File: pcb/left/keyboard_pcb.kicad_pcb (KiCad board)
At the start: 2 copper layers, 138.8 x 89.9 mm, 25 parts, among them J1 TRRS, K00 KEYSW, K01 KEYSW, K02 KEYSW, K03 KEYSW, K04 KEYSW, K05 KEYSW, K10 KEYSW, K11 KEYSW, K12 KEYSW, K13 KEYSW, K14 KEYSW, K15 KEYSW, K20 KEYSW, K21 KEYSW, K22 KEYSW, K23 KEYSW, K24 KEYSW, K25 KEYSW, K30 KEYSW, K31 KEYSW, K32 KEYSW, U2 Pico

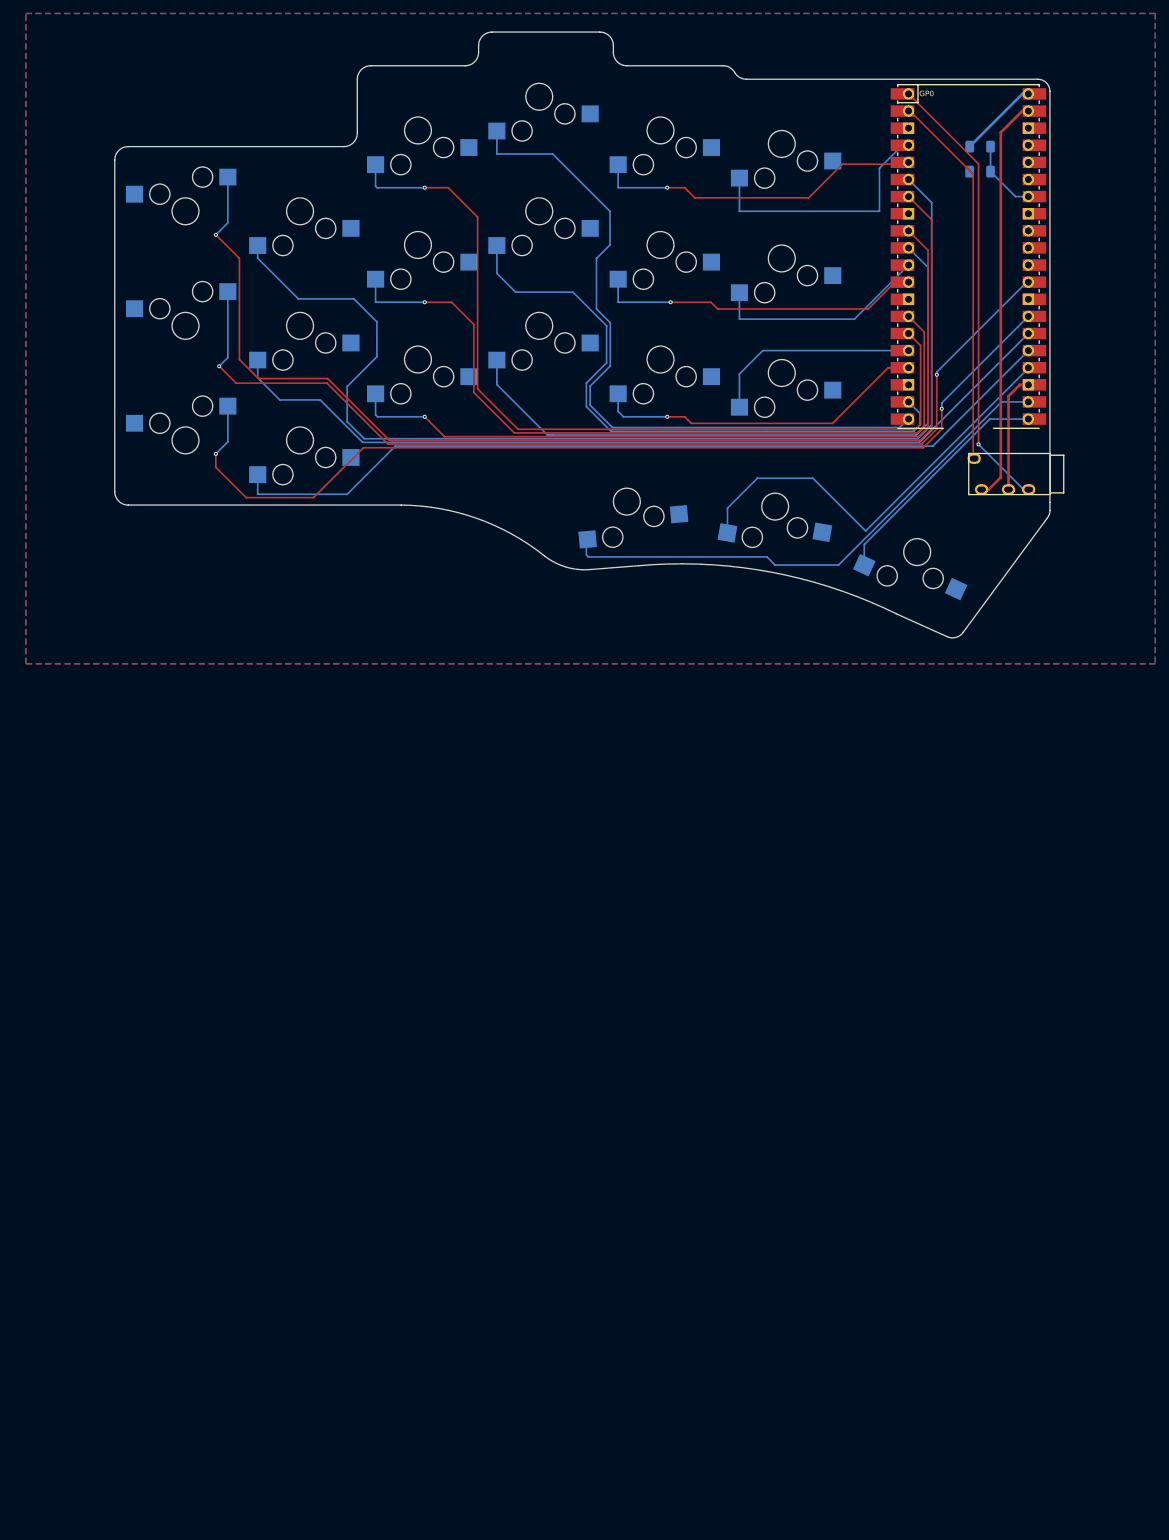
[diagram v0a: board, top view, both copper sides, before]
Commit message: feat: add right side pcb
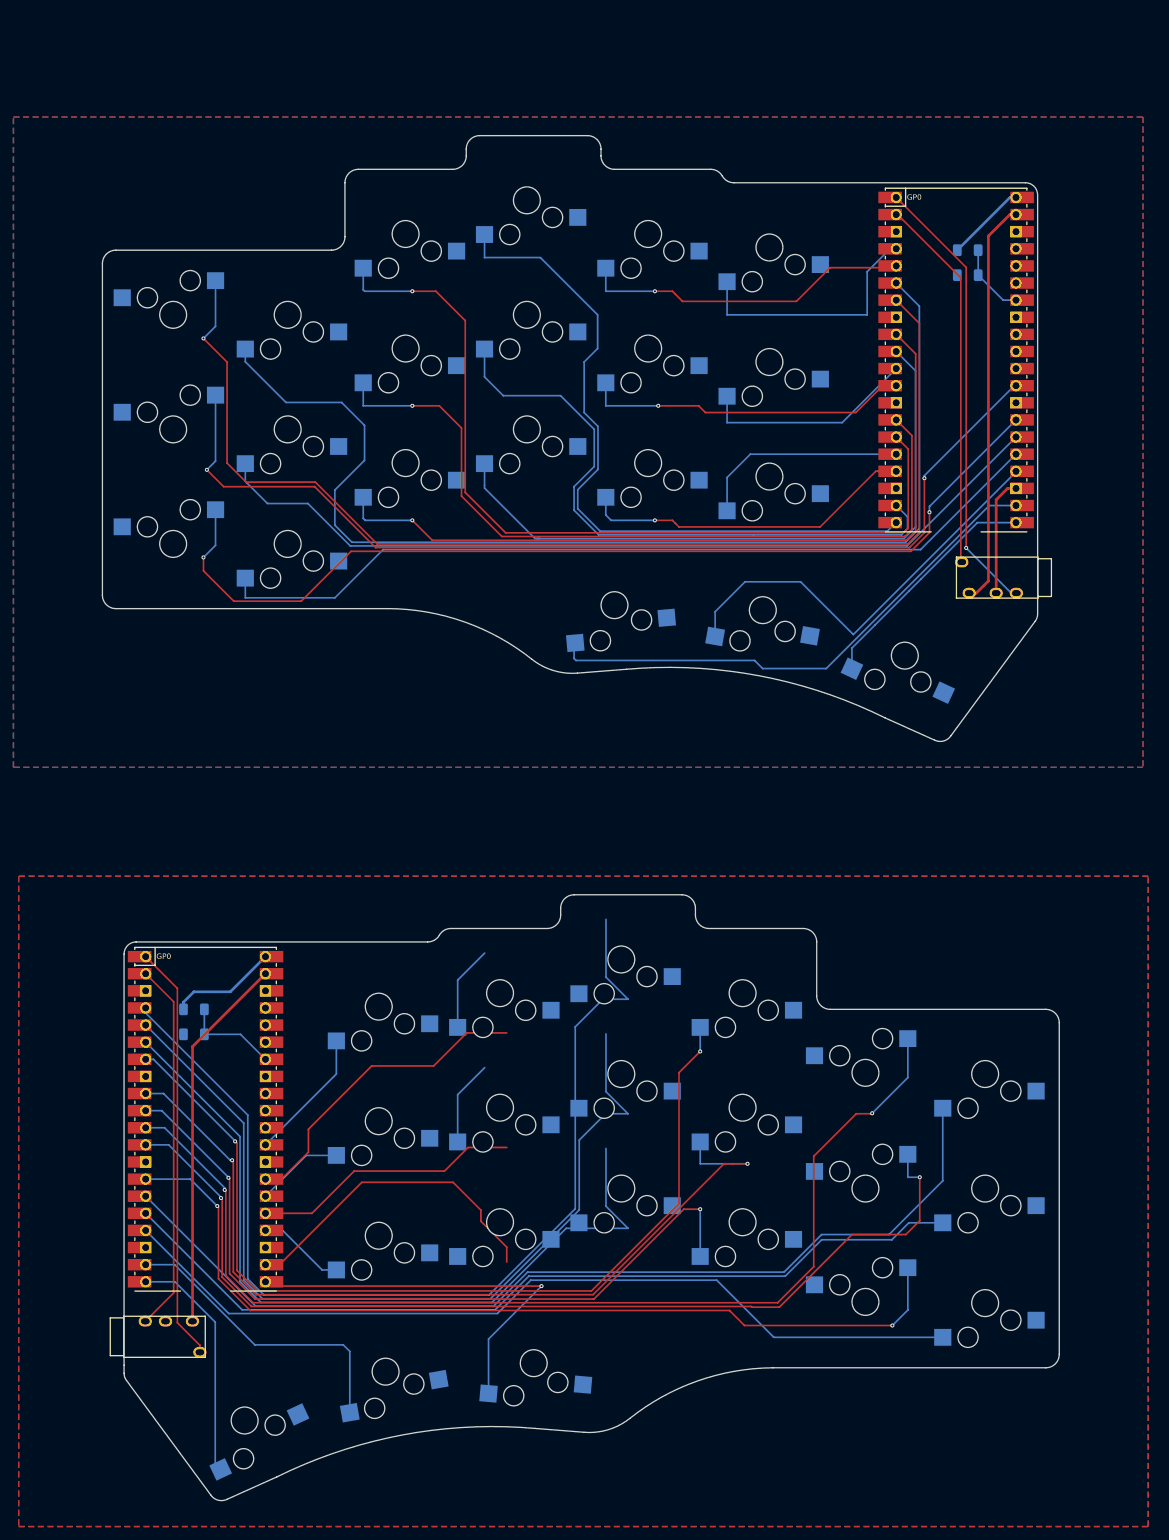
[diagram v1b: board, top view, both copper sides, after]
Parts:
- added J1: TRRS, Keebio-Parts:TRRS-PJ-320A, F.Cu at (37.4, 213.2)
- added K00: KEYSW, keyswitches:Kailh_socket_MX_3_pins_last, F.Cu at (166.3, 174.2)
- added K01: KEYSW, keyswitches:Kailh_socket_MX_3_pins_last, F.Cu at (146.5, 174.0)
- added K02: KEYSW, keyswitches:Kailh_socket_MX_3_pins_last, F.Cu at (130.3, 162.2)
- added K03: KEYSW, keyswitches:Kailh_socket_MX_3_pins_last, F.Cu at (112.3, 157.2)
- added K04: KEYSW, keyswitches:Kailh_socket_MX_3_pins_last, F.Cu at (94.3, 162.2)
- added K05: KEYSW, keyswitches:Kailh_socket_MX_3_pins_last, F.Cu at (76.3, 164.2)
- added K10: KEYSW, keyswitches:Kailh_socket_MX_3_pins_last, F.Cu at (166.3, 191.2)
- added K11: KEYSW, keyswitches:Kailh_socket_MX_3_pins_last, F.Cu at (146.5, 191.2)
- added K12: KEYSW, keyswitches:Kailh_socket_MX_3_pins_last, F.Cu at (130.3, 179.2)
- added K13: KEYSW, keyswitches:Kailh_socket_MX_3_pins_last, F.Cu at (112.3, 174.2)
- added K14: KEYSW, keyswitches:Kailh_socket_MX_3_pins_last, F.Cu at (94.3, 179.2)
- added K15: KEYSW, keyswitches:Kailh_socket_MX_3_pins_last, F.Cu at (76.3, 181.2)
- added K20: KEYSW, keyswitches:Kailh_socket_MX_3_pins_last, F.Cu at (166.3, 208.2)
- added K21: KEYSW, keyswitches:Kailh_socket_MX_3_pins_last, F.Cu at (146.5, 208.0)
- added K22: KEYSW, keyswitches:Kailh_socket_MX_3_pins_last, F.Cu at (130.3, 196.2)
- added K23: KEYSW, keyswitches:Kailh_socket_MX_3_pins_last, F.Cu at (112.3, 191.2)
- added K24: KEYSW, keyswitches:Kailh_socket_MX_3_pins_last, F.Cu at (94.3, 196.2)
- added K25: KEYSW, keyswitches:Kailh_socket_MX_3_pins_last, F.Cu at (76.3, 198.2)
- added K30: KEYSW, keyswitches:Kailh_socket_MX_3_pins_last, F.Cu at (99.3, 217.2)
- added K31: KEYSW, keyswitches:Kailh_socket_MX_3_pins_last, F.Cu at (77.3, 218.2)
- added K32: KEYSW, keyswitches:Kailh_socket_MX_3_pins_last, F.Cu at (56.3, 225.2)
- added R1: 5k6, Resistor_SMD:R_1206_3216Metric_Pad1.30x1.75mm_HandSolder, B.Cu at (47.8, 164.6)
- added R2: 10k, Resistor_SMD:R_1206_3216Metric_Pad1.30x1.75mm_HandSolder, B.Cu at (47.8, 168.3)
- added U2: Pico, RPi_Pico:RPi_Pico_SMD_TH, F.Cu at (49.6, 180.9)
- moved J1 15.5 mm to (173.1, 100.5)
- moved K20 15.5 mm to (43.8, 95.5)
- moved K21 15.5 mm to (62.8, 95.5)
- moved K22 15.5 mm to (80.2, 83.5)
- moved K24 15.5 mm to (116.2, 83.5)
- moved K25 15.5 mm to (134.2, 85.5)
- moved K30 15.5 mm to (111.2, 104.5)
- moved K31 15.5 mm to (133.2, 105.5)
- moved K32 15.5 mm to (154.2, 112.5)
- moved R1 15.5 mm to (162.7, 51.9)
- moved K00 15.5 mm to (43.8, 61.5)
- moved K01 15.5 mm to (62.8, 61.5)
- moved K02 15.5 mm to (80.2, 49.5)
- moved K03 15.5 mm to (98.2, 44.5)
- moved K04 15.5 mm to (116.2, 49.5)
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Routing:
- net /k01: track 167.1 -> 327.9 mm, vias 0 -> 2
- net /k03: track 104.6 -> 255.7 mm
- net /k11: track 127.7 -> 276.4 mm, vias 0 -> 2
- net /k00: track 173.6 -> 317.1 mm
- net /k02: track 128.5 -> 265.8 mm, vias 1 -> 3
- net /k21: track 127.3 -> 262.8 mm, vias 0 -> 2
- net /k13: track 92.4 -> 225.1 mm
- net /k12: track 116.5 -> 246.1 mm, vias 1 -> 3
- net /k10: track 151.5 -> 281.1 mm
- net /k20: track 146.7 -> 275.7 mm
- net /k23: track 99.2 -> 217.1 mm
- net /k22: track 117.4 -> 232.3 mm, vias 1 -> 3
- net tx: track 66.5 -> 128.6 mm
- net /k30: track 78.6 -> 139.1 mm, vias 0 -> 1
- net /k04: track 50.0 -> 109.5 mm
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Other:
- board size 138.8 x 89.9 mm -> 142 x 202.6 mm

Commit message: feat: update
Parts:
- moved K01 0.18 mm to (146.4, 174.2)
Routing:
- net /k03: track 255.7 -> 239.1 mm, vias 0 -> 2
- net /k13: track 225.1 -> 209.1 mm, vias 0 -> 2
- net /k23: track 217.1 -> 208.4 mm, vias 0 -> 2
- net /k04: track 109.5 -> 102.5 mm, vias 1 -> 2
- net /k14: track 101.1 -> 97.6 mm, vias 1 -> 2
- net /k24: track 100.7 -> 101.9 mm, vias 1 -> 2
